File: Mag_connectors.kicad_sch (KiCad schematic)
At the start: 3 parts

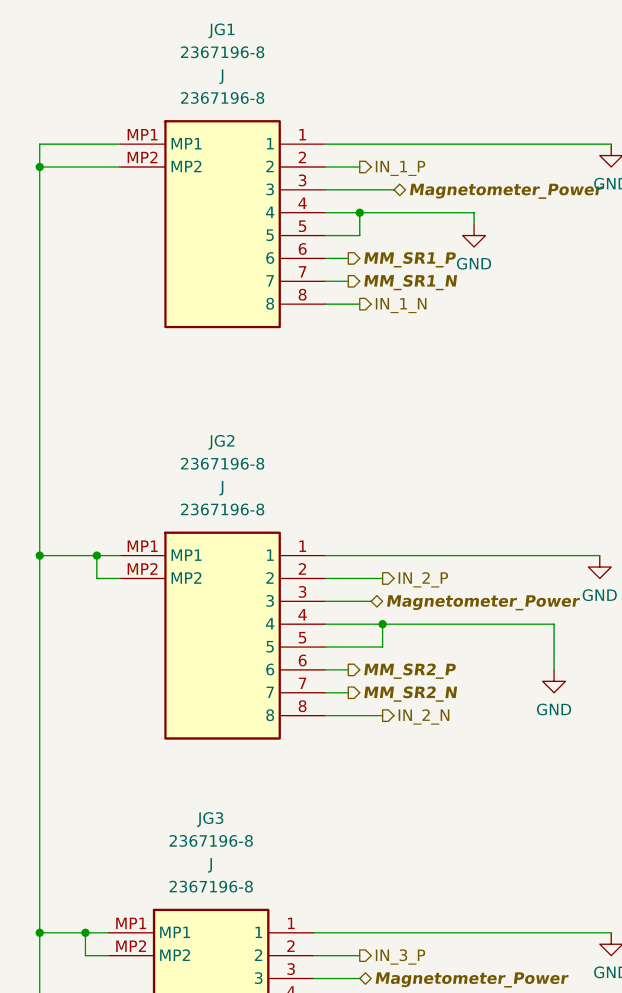
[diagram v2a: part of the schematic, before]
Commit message: Page settings changed. Added some testpoints. Some comments are made.
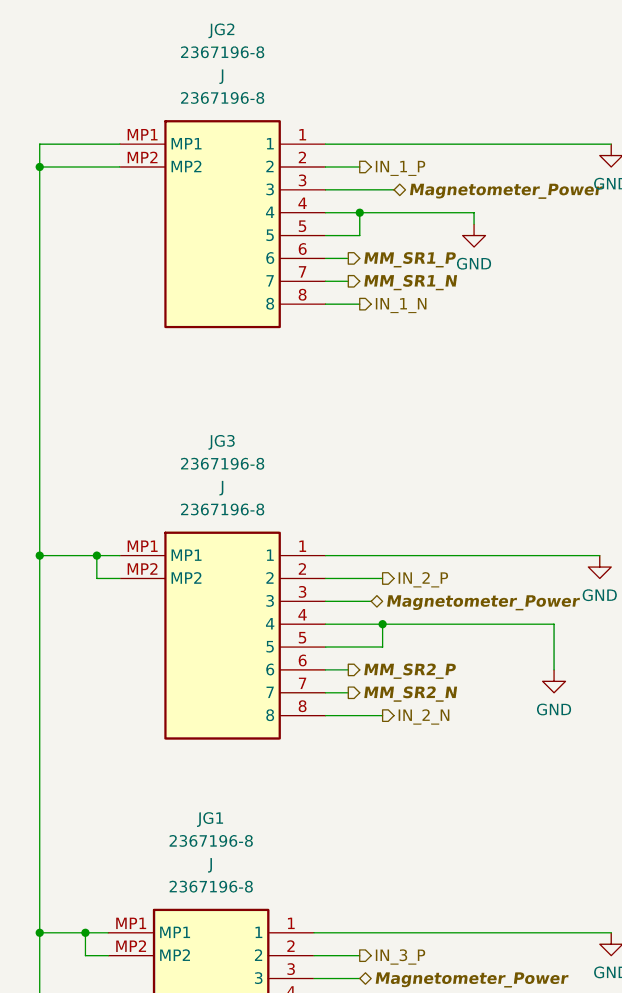
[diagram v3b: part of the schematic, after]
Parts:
- renumbered JG3 to JG1, JG1 to JG2, JG2 to JG3
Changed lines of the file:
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@@
   (symbol (lib_id "2367196-8:2367196-8") (at 54.61 95.25 0) (unit 1)
     (in_bom yes) (on_board yes) (fields_autoplaced)
-    (property "Reference" "JG2" (id 0) (at 66.04 82.55 0))
+    (property "Reference" "JG3" (id 0) (at 66.04 82.55 0))
     (property "Value" "2367196-8" (id 1) (at 66.04 85.09 0))
     (property "Footprint" "" (id 2) (at 54.61 95.25 0)
@@
   (symbol (lib_id "2367196-8:2367196-8") (at 53.34 137.16 0) (unit 1)
     (in_bom yes) (on_board yes) (fields_autoplaced)
-    (property "Reference" "JG3" (id 0) (at 64.77 124.46 0))
+    (property "Reference" "JG1" (id 0) (at 64.77 124.46 0))
     (property "Value" "2367196-8" (id 1) (at 64.77 127 0))
     (property "Footprint" "" (id 2) (at 53.34 137.16 0)
@@
   (symbol (lib_id "upsat-comms-hardware:GND") (at 109.22 49.53 0) (unit 1)
     (in_bom yes) (on_board yes) (fields_autoplaced)
-    (property "Reference" "#PWR0150" (id 0) (at 109.22 55.88 0)
+    (property "Reference" "#PWR0168" (id 0) (at 109.22 55.88 0)
       (effects (font (size 1.27 1.27)) hide)
     )
@@
   (symbol (lib_id "upsat-comms-hardware:GND") (at 102.87 107.95 0) (unit 1)
     (in_bom yes) (on_board yes) (fields_autoplaced)
-    (property "Reference" "#PWR0153" (id 0) (at 102.87 114.3 0)
+    (property "Reference" "#PWR0165" (id 0) (at 102.87 114.3 0)
       (effects (font (size 1.27 1.27)) hide)
     )
@@
   (symbol (lib_id "upsat-comms-hardware:GND") (at 102.87 152.4 0) (unit 1)
     (in_bom yes) (on_board yes) (fields_autoplaced)
-    (property "Reference" "#PWR0155" (id 0) (at 102.87 158.75 0)
+    (property "Reference" "#PWR0166" (id 0) (at 102.87 158.75 0)
       (effects (font (size 1.27 1.27)) hide)
     )
@@
   (symbol (lib_id "upsat-comms-hardware:GND") (at 45.72 154.94 0) (unit 1)
     (in_bom yes) (on_board yes) (fields_autoplaced)
-    (property "Reference" "#PWR0156" (id 0) (at 45.72 161.29 0)
+    (property "Reference" "#PWR0163" (id 0) (at 45.72 161.29 0)
       (effects (font (size 1.27 1.27)) hide)
     )
@@
   (symbol (lib_id "2367196-8:2367196-8") (at 54.61 49.53 0) (unit 1)
     (in_bom yes) (on_board yes) (fields_autoplaced)
-    (property "Reference" "JG1" (id 0) (at 66.04 36.83 0))
+    (property "Reference" "JG2" (id 0) (at 66.04 36.83 0))
     (property "Value" "2367196-8" (id 1) (at 66.04 39.37 0))
     (property "Footprint" "" (id 2) (at 54.61 49.53 0)
@@
   (symbol (lib_id "upsat-comms-hardware:GND") (at 107.95 95.25 0) (unit 1)
     (in_bom yes) (on_board yes) (fields_autoplaced)
-    (property "Reference" "#PWR0152" (id 0) (at 107.95 101.6 0)
+    (property "Reference" "#PWR0167" (id 0) (at 107.95 101.6 0)
       (effects (font (size 1.27 1.27)) hide)
     )
@@
   (symbol (lib_id "upsat-comms-hardware:GND") (at 93.98 58.42 0) (unit 1)
     (in_bom yes) (on_board yes) (fields_autoplaced)
-    (property "Reference" "#PWR0151" (id 0) (at 93.98 64.77 0)
+    (property "Reference" "#PWR0164" (id 0) (at 93.98 64.77 0)
       (effects (font (size 1.27 1.27)) hide)
     )
@@
   (symbol (lib_id "upsat-comms-hardware:GND") (at 109.22 137.16 0) (unit 1)
     (in_bom yes) (on_board yes) (fields_autoplaced)
-    (property "Reference" "#PWR0154" (id 0) (at 109.22 143.51 0)
+    (property "Reference" "#PWR0169" (id 0) (at 109.22 143.51 0)
       (effects (font (size 1.27 1.27)) hide)
     )

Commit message: I2C lines are pulled up
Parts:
- JG1, JG2, JG3: footprint (none) -> 2367196-8:23671968
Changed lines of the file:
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@@
     (property "Reference" "JG3" (id 0) (at 66.04 82.55 0))
     (property "Value" "2367196-8" (id 1) (at 66.04 85.09 0))
-    (property "Footprint" "" (id 2) (at 54.61 95.25 0)
+    (property "Footprint" "2367196-8:23671968" (id 2) (at 54.61 95.25 0)
       (effects (font (size 1.27 1.27)) hide)
     )
@@
     (property "Reference" "JG1" (id 0) (at 64.77 124.46 0))
     (property "Value" "2367196-8" (id 1) (at 64.77 127 0))
-    (property "Footprint" "" (id 2) (at 53.34 137.16 0)
+    (property "Footprint" "2367196-8:23671968" (id 2) (at 53.34 137.16 0)
       (effects (font (size 1.27 1.27)) hide)
     )
@@
   (symbol (lib_id "upsat-comms-hardware:GND") (at 109.22 49.53 0) (unit 1)
     (in_bom yes) (on_board yes) (fields_autoplaced)
-    (property "Reference" "#PWR0168" (id 0) (at 109.22 55.88 0)
+    (property "Reference" "#PWR0170" (id 0) (at 109.22 55.88 0)
       (effects (font (size 1.27 1.27)) hide)
     )
@@
   (symbol (lib_id "upsat-comms-hardware:GND") (at 102.87 107.95 0) (unit 1)
     (in_bom yes) (on_board yes) (fields_autoplaced)
-    (property "Reference" "#PWR0165" (id 0) (at 102.87 114.3 0)
+    (property "Reference" "#PWR0167" (id 0) (at 102.87 114.3 0)
       (effects (font (size 1.27 1.27)) hide)
     )
@@
   (symbol (lib_id "upsat-comms-hardware:GND") (at 102.87 152.4 0) (unit 1)
     (in_bom yes) (on_board yes) (fields_autoplaced)
-    (property "Reference" "#PWR0166" (id 0) (at 102.87 158.75 0)
+    (property "Reference" "#PWR0168" (id 0) (at 102.87 158.75 0)
       (effects (font (size 1.27 1.27)) hide)
     )
@@
   (symbol (lib_id "upsat-comms-hardware:GND") (at 45.72 154.94 0) (unit 1)
     (in_bom yes) (on_board yes) (fields_autoplaced)
-    (property "Reference" "#PWR0163" (id 0) (at 45.72 161.29 0)
+    (property "Reference" "#PWR0165" (id 0) (at 45.72 161.29 0)
       (effects (font (size 1.27 1.27)) hide)
     )
@@
     (property "Reference" "JG2" (id 0) (at 66.04 36.83 0))
     (property "Value" "2367196-8" (id 1) (at 66.04 39.37 0))
-    (property "Footprint" "" (id 2) (at 54.61 49.53 0)
+    (property "Footprint" "2367196-8:23671968" (id 2) (at 54.61 49.53 0)
       (effects (font (size 1.27 1.27)) hide)
     )
@@
   (symbol (lib_id "upsat-comms-hardware:GND") (at 107.95 95.25 0) (unit 1)
     (in_bom yes) (on_board yes) (fields_autoplaced)
-    (property "Reference" "#PWR0167" (id 0) (at 107.95 101.6 0)
+    (property "Reference" "#PWR0169" (id 0) (at 107.95 101.6 0)
       (effects (font (size 1.27 1.27)) hide)
     )
@@
   (symbol (lib_id "upsat-comms-hardware:GND") (at 93.98 58.42 0) (unit 1)
     (in_bom yes) (on_board yes) (fields_autoplaced)
-    (property "Reference" "#PWR0164" (id 0) (at 93.98 64.77 0)
+    (property "Reference" "#PWR0166" (id 0) (at 93.98 64.77 0)
       (effects (font (size 1.27 1.27)) hide)
     )
@@
   (symbol (lib_id "upsat-comms-hardware:GND") (at 109.22 137.16 0) (unit 1)
     (in_bom yes) (on_board yes) (fields_autoplaced)
-    (property "Reference" "#PWR0169" (id 0) (at 109.22 143.51 0)
+    (property "Reference" "#PWR0171" (id 0) (at 109.22 143.51 0)
       (effects (font (size 1.27 1.27)) hide)
     )

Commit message: Final Schematic
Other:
- note removed: "Check hmc 1051 pinout, lets keep two test points for the offset strap"
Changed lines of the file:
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@@
     (stroke (width 0) (type default) (color 0 0 0 0))
-  )
-  (text "Check hmc 1051 \npinout, \nlets keep two test \npoints for the offset strap \n"
-    (at 154.94 76.2 0)
-    (effects (font (size 1.27 1.27)) (justify left bottom))
   )
   (hierarchical_label "MM_SR3_P" (shape output) (at 81.28 149.86 0)

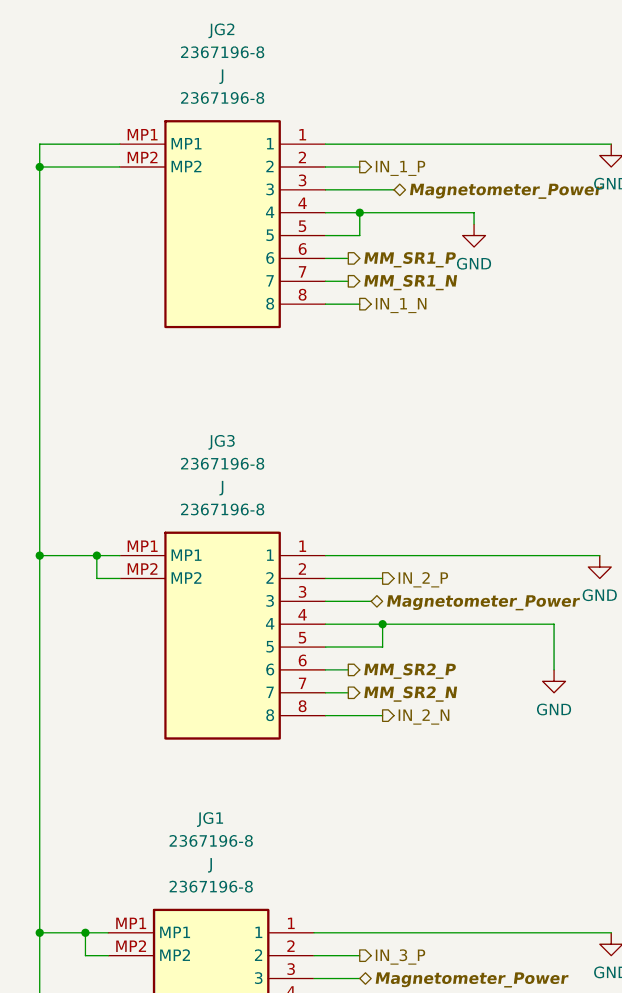
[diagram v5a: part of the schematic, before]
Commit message: MCU circuitry forgot LOL
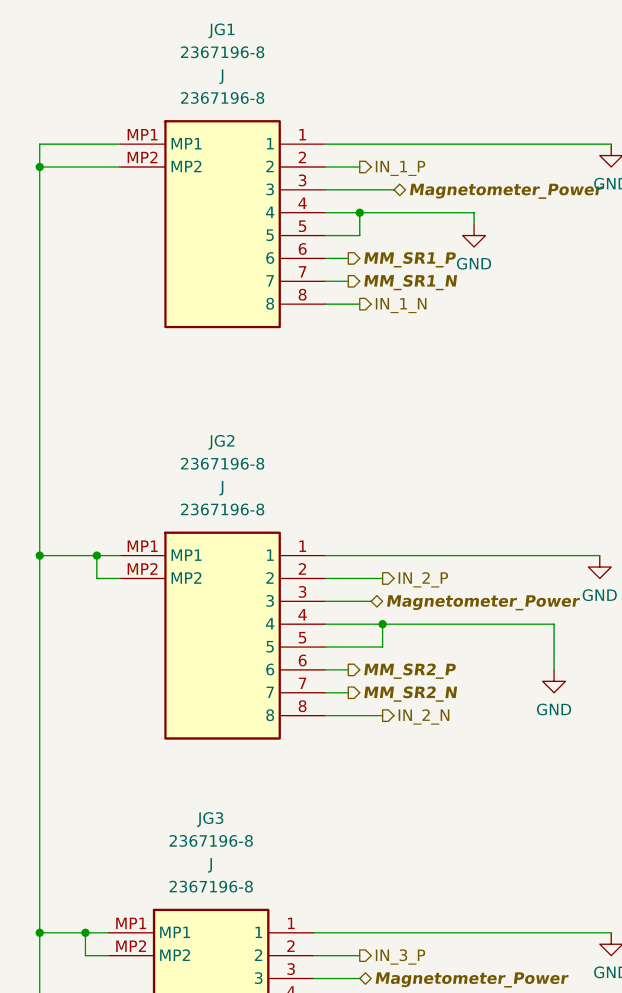
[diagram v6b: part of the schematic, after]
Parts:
- renumbered JG2 to JG1, JG3 to JG2, JG1 to JG3
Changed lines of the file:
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@@
   (symbol (lib_id "2367196-8:2367196-8") (at 54.61 95.25 0) (unit 1)
     (in_bom yes) (on_board yes) (fields_autoplaced)
-    (property "Reference" "JG3" (id 0) (at 66.04 82.55 0))
+    (property "Reference" "JG2" (id 0) (at 66.04 82.55 0))
     (property "Value" "2367196-8" (id 1) (at 66.04 85.09 0))
     (property "Footprint" "2367196-8:23671968" (id 2) (at 54.61 95.25 0)
@@
   (symbol (lib_id "2367196-8:2367196-8") (at 53.34 137.16 0) (unit 1)
     (in_bom yes) (on_board yes) (fields_autoplaced)
-    (property "Reference" "JG1" (id 0) (at 64.77 124.46 0))
+    (property "Reference" "JG3" (id 0) (at 64.77 124.46 0))
     (property "Value" "2367196-8" (id 1) (at 64.77 127 0))
     (property "Footprint" "2367196-8:23671968" (id 2) (at 53.34 137.16 0)
@@
   (symbol (lib_id "upsat-comms-hardware:GND") (at 109.22 49.53 0) (unit 1)
     (in_bom yes) (on_board yes) (fields_autoplaced)
-    (property "Reference" "#PWR0170" (id 0) (at 109.22 55.88 0)
+    (property "Reference" "#PWR0172" (id 0) (at 109.22 55.88 0)
       (effects (font (size 1.27 1.27)) hide)
     )
@@
   (symbol (lib_id "upsat-comms-hardware:GND") (at 102.87 107.95 0) (unit 1)
     (in_bom yes) (on_board yes) (fields_autoplaced)
-    (property "Reference" "#PWR0167" (id 0) (at 102.87 114.3 0)
+    (property "Reference" "#PWR0175" (id 0) (at 102.87 114.3 0)
       (effects (font (size 1.27 1.27)) hide)
     )
@@
   (symbol (lib_id "upsat-comms-hardware:GND") (at 102.87 152.4 0) (unit 1)
     (in_bom yes) (on_board yes) (fields_autoplaced)
-    (property "Reference" "#PWR0168" (id 0) (at 102.87 158.75 0)
+    (property "Reference" "#PWR0177" (id 0) (at 102.87 158.75 0)
       (effects (font (size 1.27 1.27)) hide)
     )
@@
   (symbol (lib_id "upsat-comms-hardware:GND") (at 45.72 154.94 0) (unit 1)
     (in_bom yes) (on_board yes) (fields_autoplaced)
-    (property "Reference" "#PWR0165" (id 0) (at 45.72 161.29 0)
+    (property "Reference" "#PWR0178" (id 0) (at 45.72 161.29 0)
       (effects (font (size 1.27 1.27)) hide)
     )
@@
   (symbol (lib_id "2367196-8:2367196-8") (at 54.61 49.53 0) (unit 1)
     (in_bom yes) (on_board yes) (fields_autoplaced)
-    (property "Reference" "JG2" (id 0) (at 66.04 36.83 0))
+    (property "Reference" "JG1" (id 0) (at 66.04 36.83 0))
     (property "Value" "2367196-8" (id 1) (at 66.04 39.37 0))
     (property "Footprint" "2367196-8:23671968" (id 2) (at 54.61 49.53 0)
@@
   (symbol (lib_id "upsat-comms-hardware:GND") (at 107.95 95.25 0) (unit 1)
     (in_bom yes) (on_board yes) (fields_autoplaced)
-    (property "Reference" "#PWR0169" (id 0) (at 107.95 101.6 0)
+    (property "Reference" "#PWR0174" (id 0) (at 107.95 101.6 0)
       (effects (font (size 1.27 1.27)) hide)
     )
@@
   (symbol (lib_id "upsat-comms-hardware:GND") (at 93.98 58.42 0) (unit 1)
     (in_bom yes) (on_board yes) (fields_autoplaced)
-    (property "Reference" "#PWR0166" (id 0) (at 93.98 64.77 0)
+    (property "Reference" "#PWR0173" (id 0) (at 93.98 64.77 0)
       (effects (font (size 1.27 1.27)) hide)
     )
@@
   (symbol (lib_id "upsat-comms-hardware:GND") (at 109.22 137.16 0) (unit 1)
     (in_bom yes) (on_board yes) (fields_autoplaced)
-    (property "Reference" "#PWR0171" (id 0) (at 109.22 143.51 0)
+    (property "Reference" "#PWR0176" (id 0) (at 109.22 143.51 0)
       (effects (font (size 1.27 1.27)) hide)
     )
